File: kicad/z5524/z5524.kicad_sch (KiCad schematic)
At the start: 47 parts, among them J1 Conn_01x01, J2 Conn_02x20_Odd_Even, J3 Conn_01x02, J4 Conn_01x01, Q2 MMBT3904, U10 LM337L_TO92, U11 DG442xY, U12 PCA9555D, U14 TL072, U19 LM4040BIM3-4.1, U20 M24C02-WMN, U4 LM4040BIM3-2.5, U8 TL074, U9 LM78L05_TO92

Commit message: reannotate geographically
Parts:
- renumbered C24 to C30, C26 to C31, C30 to C32, C40 to C36, C43 to C42, C48 to C46, C55 to C53, C62 to C58, C59 to C61, C64 to C63, D8 to D6, J4 to J1, J1 to J2, J2 to J3, J3 to J4, R99 to R102, R97 to R103, R98 to R104, R100 to R106, R13 to R16, R44 to R46, R33 to R47, R53 to R58, R58 to R60, R56 to R61, R59 to R63, R66 to R70, R67 to R71, R94 to R98, U12 to U11, U11 to U13, U4 to U5

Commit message: minor rework
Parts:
- R98: value 1k -> 680; LCSC C21190 -> C23228
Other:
- note added: "VREF_4.096 load: 3.8k: 500 < Rs < 864 for current thru LM4040 of: 1000uA to 75uA"
- note removed: "VREF_4.096 load: 10k 641 < Rs < 1863 for current 1000uA : 75uA"
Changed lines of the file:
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@@
     (stroke (width 0) (type default))
   )
-  (text "VREF_4.096 load: 10k\n641 < Rs < 1863\nfor current 1000uA : 75uA"
-    (at 158.75 265.43 0)
+  (text "VREF_4.096 load: 3.8k:  500 < Rs < 864\nfor current thru LM4040 of: 1000uA to 75uA"
+    (at 150.495 264.16 0)
     (effects (font (size 1.27 1.27)) (justify left bottom))
   )
@@
   (symbol (lib_id "Device:R") (at 168.91 234.95 0) (unit 1)
     (in_bom yes) (on_board yes) (dnp no)
-    (property "Reference" "R98" (at 171.45 233.68 0)
-      (effects (font (size 1.27 1.27)))
-    )
-    (property "Value" "1k" (at 171.45 236.22 0)
+    (property "Reference" "R98" (at 172.085 233.68 0)
+      (effects (font (size 1.27 1.27)))
+    )
+    (property "Value" "680" (at 172.085 236.22 0)
       (effects (font (size 1.27 1.27)))
     )
@@
       (effects (font (size 1.27 1.27)) hide)
     )
-    (property "LCSC" "C21190" (at 168.91 234.95 0)
-      (effects (font (size 1.27 1.27)) hide)
-    )
+    (property "LCSC" "C23228" (at 168.91 234.95 0)
+      (effects (font (size 1.27 1.27)) hide)
+    )

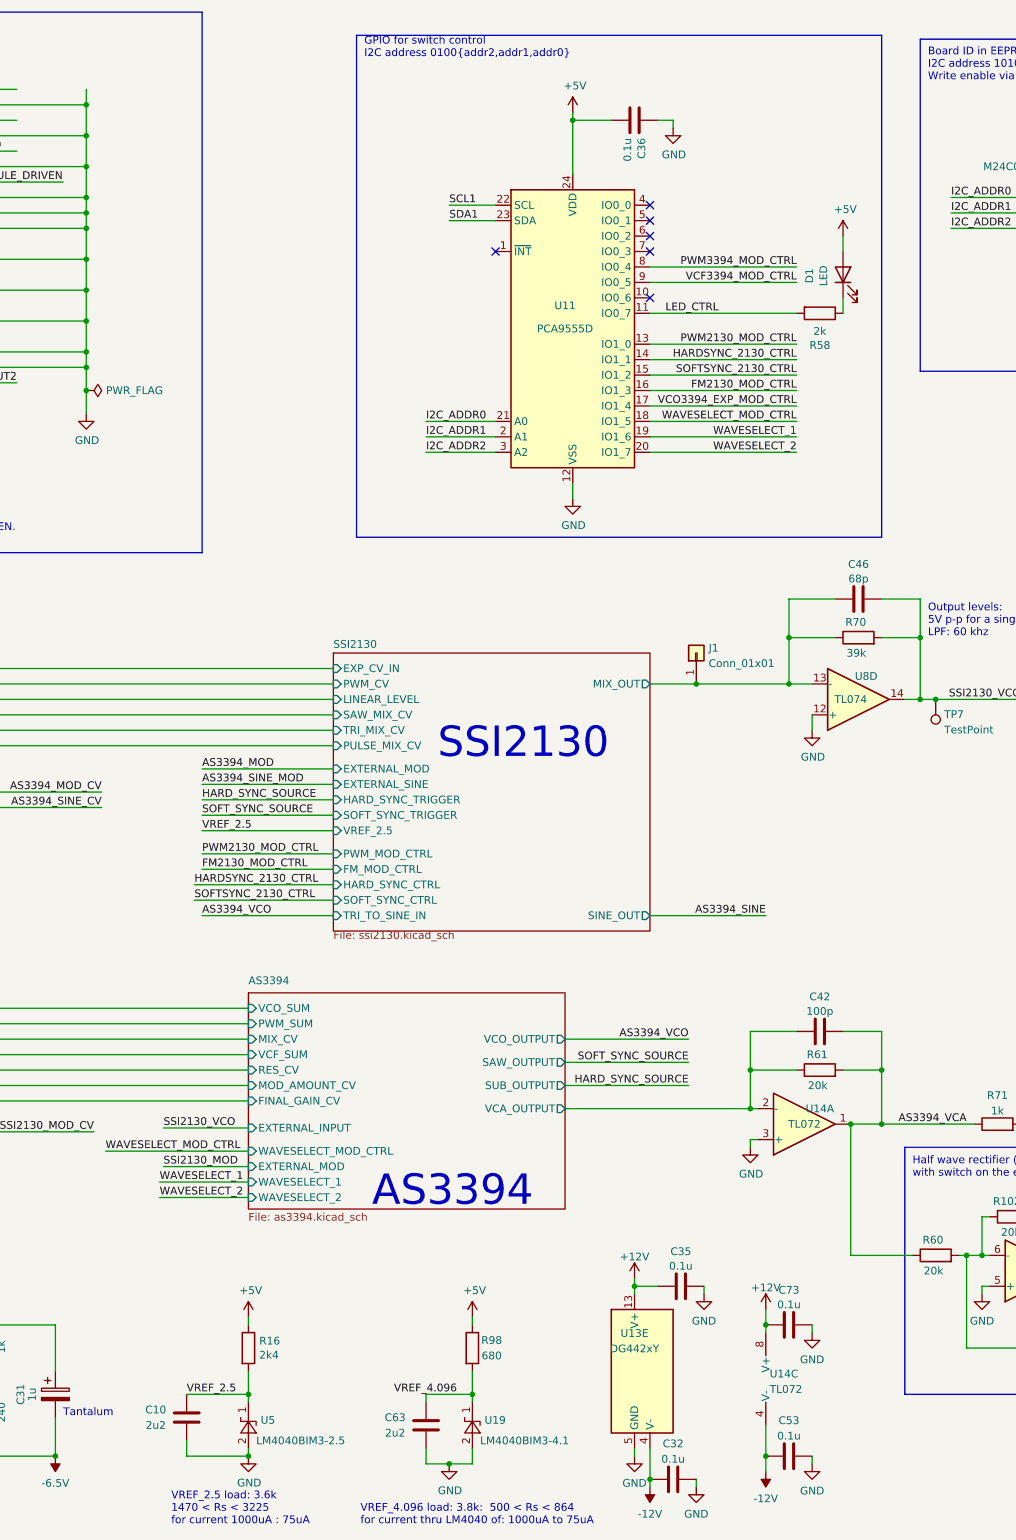
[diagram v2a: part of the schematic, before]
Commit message: fix BOM for current JLC catalog
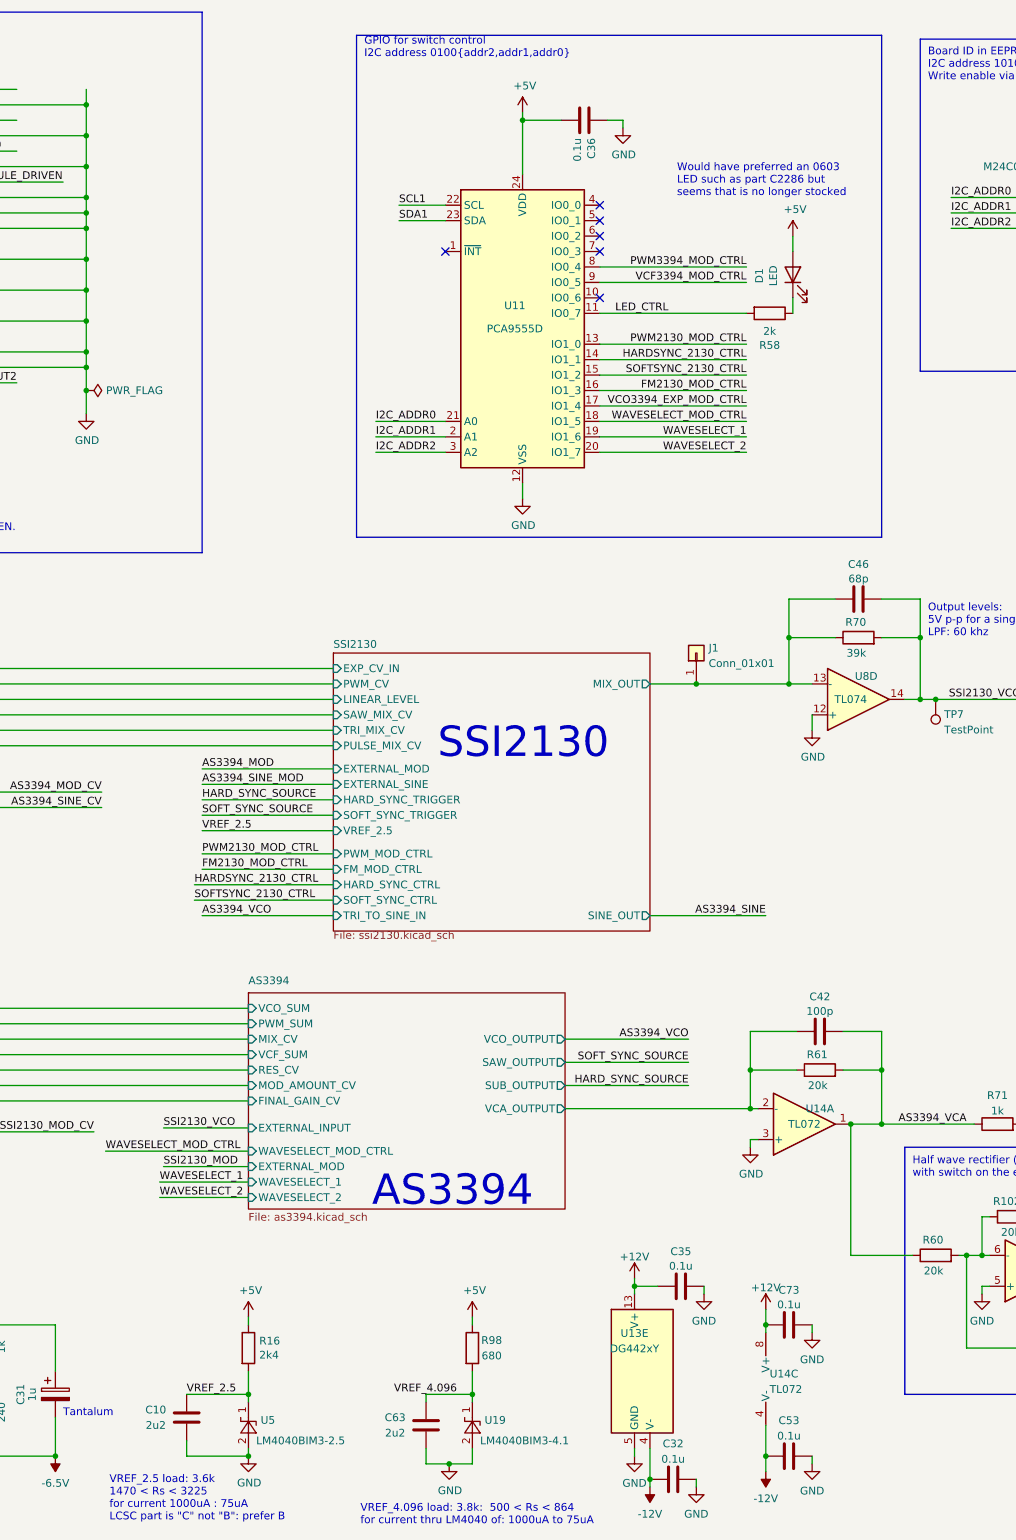
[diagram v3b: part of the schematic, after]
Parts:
- D1: footprint LED_SMD:LED_0603_1608Metric -> LED_SMD:LED_0805_2012Metric; LCSC C2286 -> C84256
- U5: LCSC C460725 -> C460607
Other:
- note added: "VREF_2.5 load: 3.6k 1470 < Rs < 3225 for current 1000uA : 75uA LCSC part is "C" not "B": prefer B"
- note added: "Would have preferred an 0603 LED such as part C2286 but seems that is no longer stocked"
- note removed: "VREF_2.5 load: 3.6k 1470 < Rs < 3225 for current 1000uA : 75uA"
- moved on the sheet: C36, D1, R58, U11

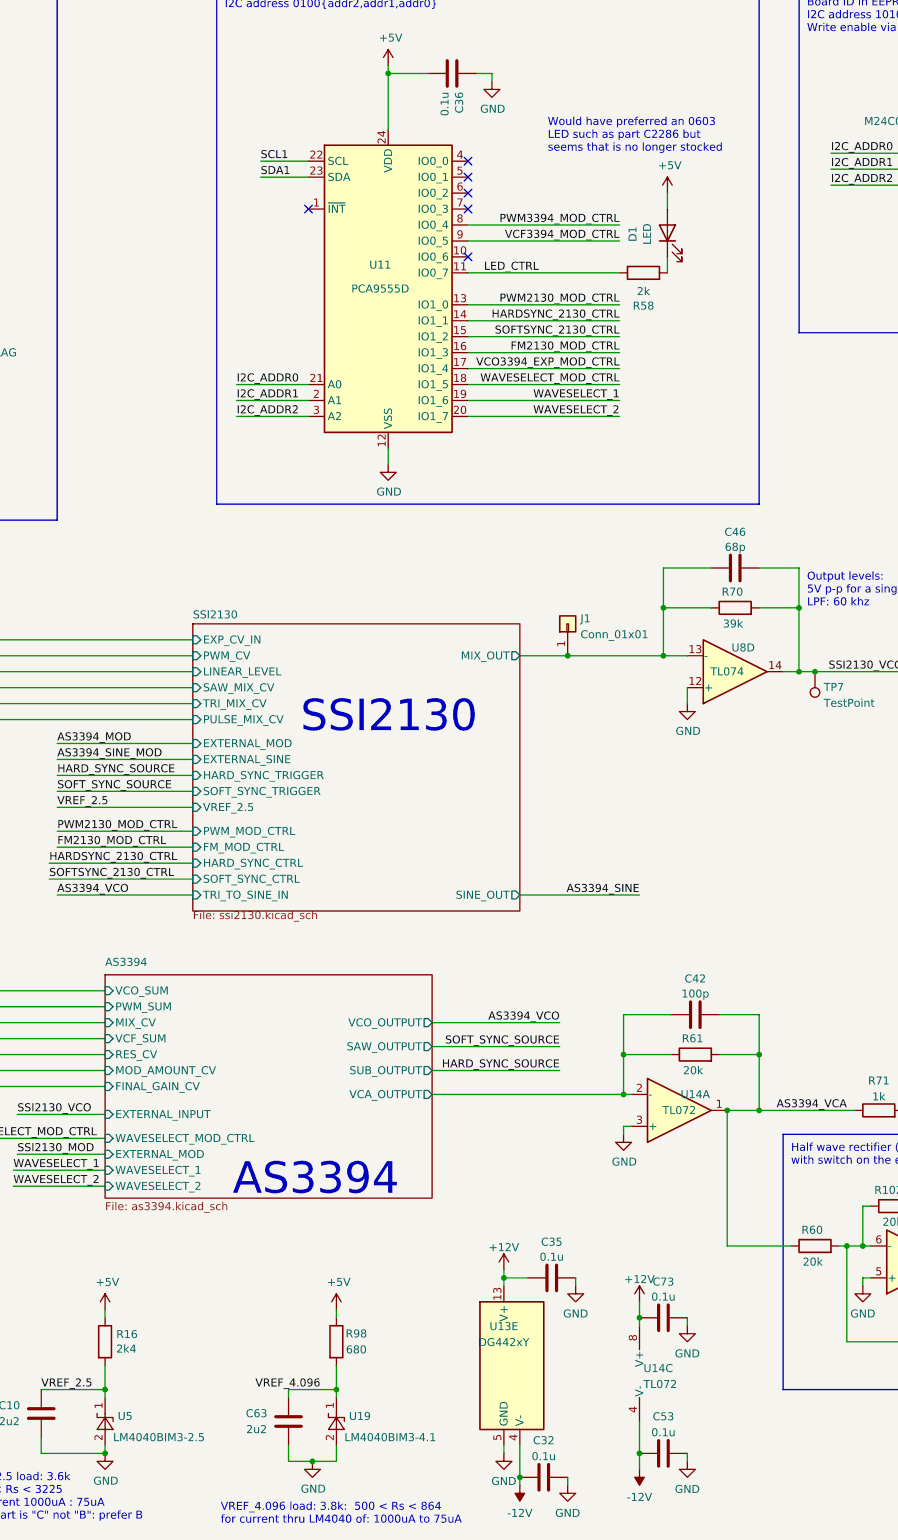
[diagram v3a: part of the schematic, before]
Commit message: some routing updates
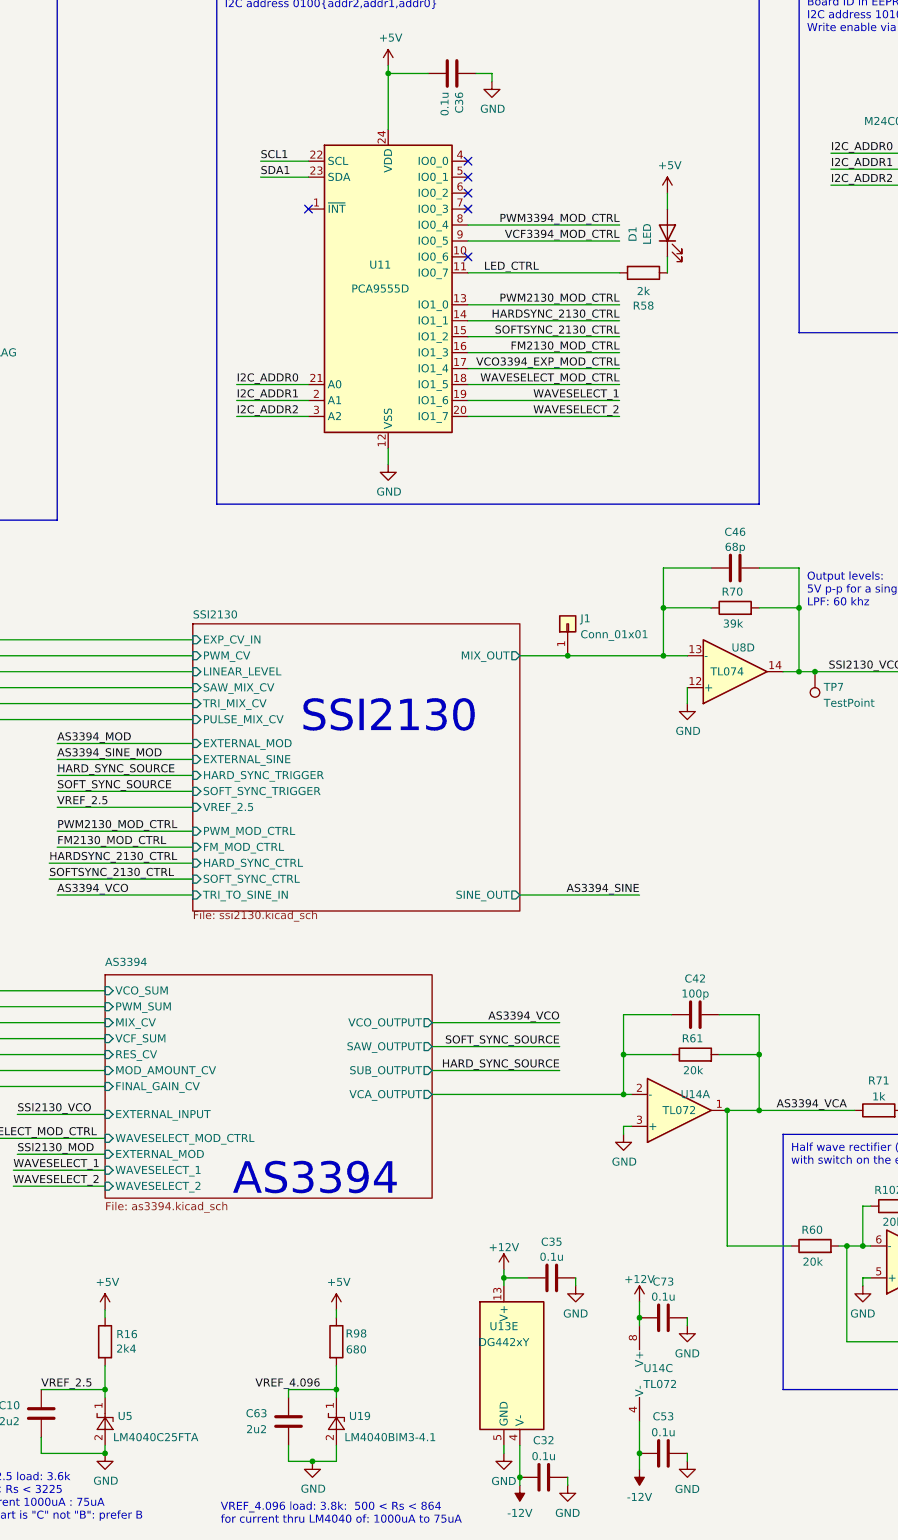
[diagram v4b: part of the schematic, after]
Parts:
- D1: footprint LED_SMD:LED_0805_2012Metric -> LED_SMD:LED_0603_1608Metric; LCSC C84256 -> C2286
- U5: value LM4040BIM3-2.5 -> LM4040C25FTA
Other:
- note removed: "Would have preferred an 0603 LED such as part C2286 but seems that is no longer stocked"
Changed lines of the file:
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@@
     (stroke (width 0) (type default))
-  )
-  (text "Would have preferred an 0603\nLED such as part C2286 but\nseems that is no longer stocked"
-    (at 202.565 45.72 0)
-    (effects (font (size 1.27 1.27)) (justify left bottom))
   )
   (text "VREF_4.096 load: 3.8k:  500 < Rs < 864\nfor current thru LM4040 of: 1000uA to 75uA"
@@
       (effects (font (size 1.27 1.27)))
     )
-    (property "Footprint" "LED_SMD:LED_0805_2012Metric" (at 221.615 58.42 0)
+    (property "Footprint" "LED_SMD:LED_0603_1608Metric" (at 221.615 58.42 0)
       (effects (font (size 1.27 1.27)) hide)
     )
@@
       (effects (font (size 1.27 1.27)) hide)
     )
-    (property "LCSC" "C84256" (at 221.615 58.42 0)
+    (property "LCSC" "C2286" (at 221.615 58.42 0)
       (effects (font (size 1.27 1.27)) hide)
     )
@@
       (effects (font (size 1.27 1.27)) (justify right))
     )
-    (property "Value" "LM4040BIM3-2.5" (at 133.35 250.19 90)
+    (property "Value" "LM4040C25FTA" (at 133.35 250.19 90)
       (effects (font (size 1.27 1.27)) (justify right))
     )
@@
       (effects (font (size 1.27 1.27) italic) hide)
     )
-    (property "Datasheet" "http://www.ti.com/lit/ds/symlink/lm4040-n.pdf" (at 132.08 247.65 0)
+    (property "Datasheet" "https://datasheet.lcsc.com/lcsc/1912111437_Diodes-Incorporated-LM4040C25FTA_C460607.pdf" (at 132.08 247.65 0)
       (effects (font (size 1.27 1.27) italic) hide)
     )

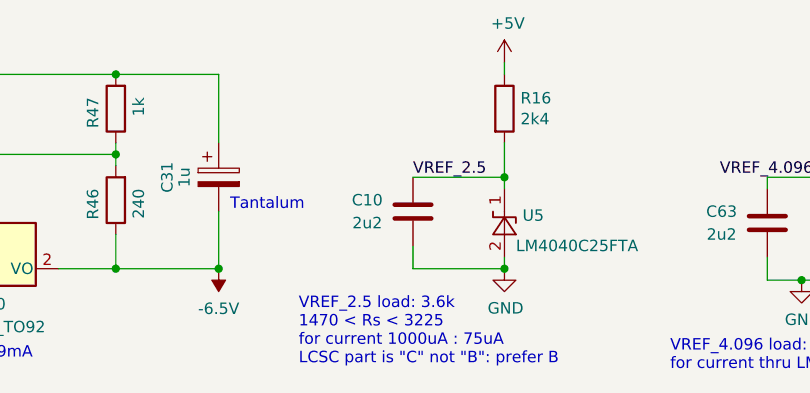
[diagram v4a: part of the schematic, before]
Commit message: updated 3394 --> 2130 FM to much deeper.  Started addressing PWM range for increased modulation
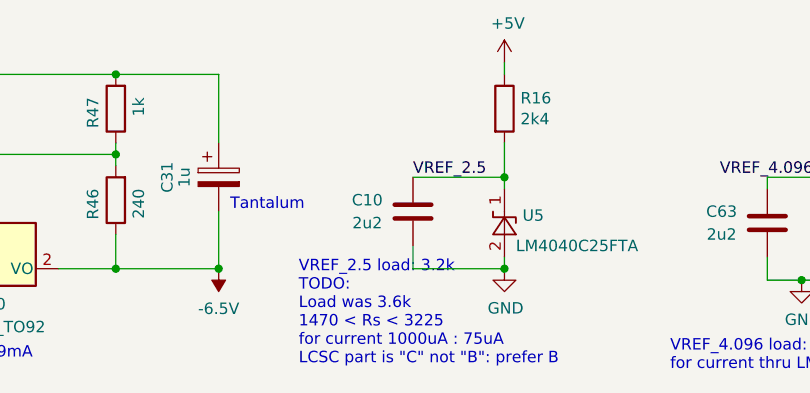
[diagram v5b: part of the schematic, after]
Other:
- note added: "VREF_2.5 load: 3.2k TODO: Load was 3.6k 1470 < Rs < 3225 for current 1000uA : 75uA LCSC part is "C" not "B": prefer B"
- note removed: "VREF_2.5 load: 3.6k 1470 < Rs < 3225 for current 1000uA : 75uA LCSC part is "C" not "B": prefer B"
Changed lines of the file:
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@@
     (effects (font (size 5.0038 5.0038)) (justify left bottom))
   )
-  (text "VREF_2.5 load: 3.6k\n1470 < Rs < 3225\nfor current 1000uA : 75uA\nLCSC part is \"C\" not \"B\": prefer B"
+  (text "VREF_2.5 load: 3.2k\nTODO:\nLoad was 3.6k\n1470 < Rs < 3225\nfor current 1000uA : 75uA\nLCSC part is \"C\" not \"B\": prefer B"
     (at 109.22 263.525 0)
     (effects (font (size 1.27 1.27)) (justify left bottom))

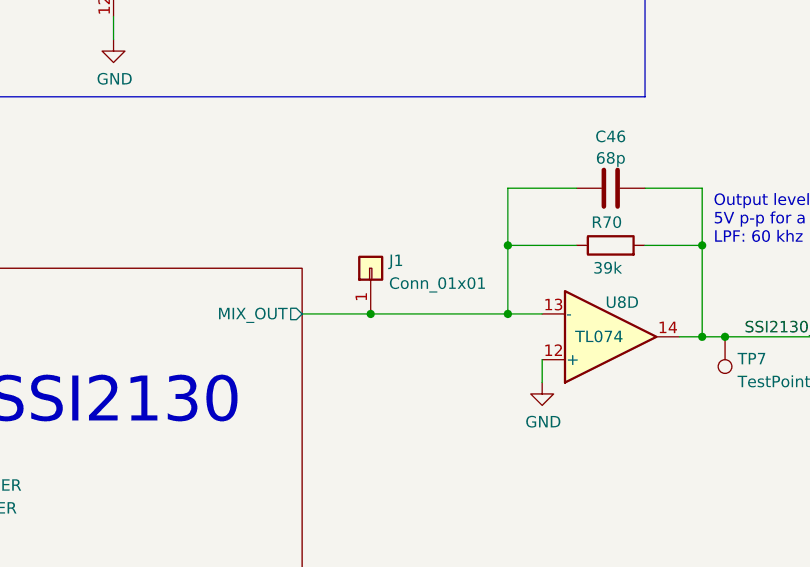
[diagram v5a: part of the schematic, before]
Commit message: fix 2130 exp pitch input and save an opamp
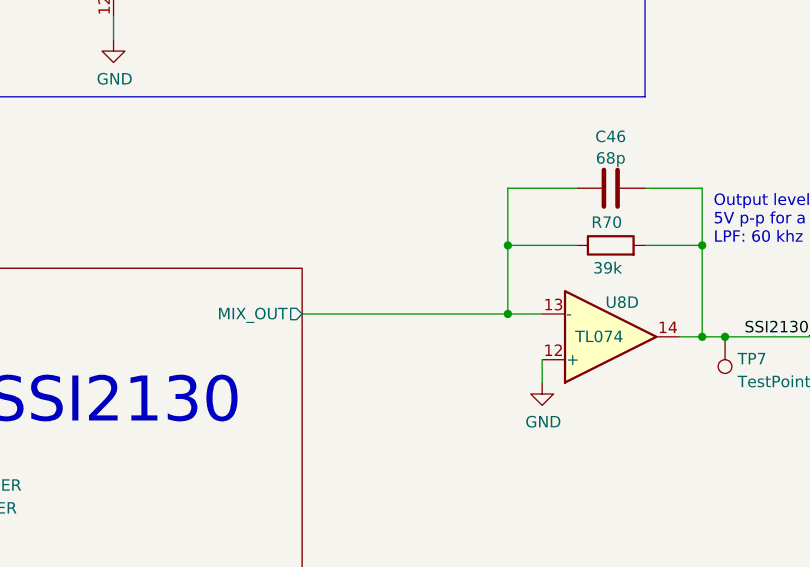
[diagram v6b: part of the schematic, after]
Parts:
- removed J1: Conn_01x01, Connector_PinHeader_2.54mm:PinHeader_1x01_P2.54mm_Vertical, symbol Connector_Generic:Conn_01x01
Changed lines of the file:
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@@
   (junction (at 105.41 71.12) (diameter 0) (color 0 0 0 0)
   )
-  (junction (at 205.74 125.73) (diameter 0) (color 0 0 0 0)
-  )
   (junction (at 242.57 118.11) (diameter 0) (color 0 0 0 0)
   )
@@
     (stroke (width 0) (type default))
   )
-  (wire (pts (xy 307.34 160.02) (xy 331.47 160.02))
-    (stroke (width 0) (type default))
-  )
   (wire (pts (xy 93.98 76.2) (xy 78.74 76.2))
     (stroke (width 0) (type default))
@@
     (stroke (width 0) (type default))
   )
-  (wire (pts (xy 205.74 125.73) (xy 220.98 125.73))
+  (wire (pts (xy 198.12 125.73) (xy 220.98 125.73))
     (stroke (width 0) (type default))
   )
@@
     (stroke (width 0) (type default))
   )
+  (wire (pts (xy 307.34 160.02) (xy 331.47 160.02))
+    (stroke (width 0) (type default))
+  )
   (wire (pts (xy 250.19 219.71) (xy 252.73 219.71))
     (stroke (width 0) (type default))
@@
     (stroke (width 0) (type default))
   )
-  (wire (pts (xy 198.12 125.73) (xy 205.74 125.73))
-    (stroke (width 0) (type default))
-  )
   (wire (pts (xy 13.97 191.77) (xy 38.1 191.77))
     (stroke (width 0) (type default))
@@
     )
   )
-  (symbol (lib_id "Connector_Generic:Conn_01x01") (at 205.74 120.65 90) (unit 1)
-    (in_bom yes) (on_board yes) (dnp no) (fields_autoplaced)
-    (property "Reference" "J1" (at 207.772 119.8153 90)
-      (effects (font (size 1.27 1.27)) (justify right))
-    )
-    (property "Value" "Conn_01x01" (at 207.772 122.3522 90)
-      (effects (font (size 1.27 1.27)) (justify right))
-    )
-    (property "Footprint" "Connector_PinHeader_2.54mm:PinHeader_1x01_P2.54mm_Vertical" (at 205.74 120.65 0)
-      (effects (font (size 1.27 1.27)) hide)
-    )
-    (property "Datasheet" "~" (at 205.74 120.65 0)
-      (effects (font (size 1.27 1.27)) hide)
-    )
-    (pin "1")
-    (instances
-      (project "z5524"
-        (path "/7079bdb0-a00e-4bac-b257-cbcf2c91bbd6"
-          (reference "J1") (unit 1)
-        )
-      )
-    )
-  )
   (symbol (lib_id "power:GND") (at 207.01 226.06 0) (unit 1)
     (in_bom yes) (on_board yes) (dnp no) (fields_autoplaced)
@@
       (effects (font (size 1.27 1.27) italic) (justify left) hide)
     )
-    (property "Datasheet" "https://www.onsemi.com/pub/Collateral/2N3903-D.PDF" (at 294.64 226.06 0)
+    (property "Datasheet" "https://www.onsemi.com/pdf/datasheet/pzt3904-d.pdf" (at 294.64 226.06 0)
       (effects (font (size 1.27 1.27)) (justify left) hide)
     )
